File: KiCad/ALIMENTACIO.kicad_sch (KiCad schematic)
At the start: 9 parts, among them J1 Conn_01x02_Pin, U1 LM2596S-5, U2 LM1117DT-3.3

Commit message: Canvis a la part d'alimentació
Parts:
- L1: value 33uH -> 100uH
- renumbered C2 to C3, U2 to U1
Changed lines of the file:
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@@
 		)
 		(instances
+			(project "ALIMENTACIO"
+				(path "/45cfcaa5-e694-40cb-923c-70f0cad76365"
+					(reference "C3")
+					(unit 1)
+				)
+			)
 			(project ""
 				(path "/b6401b4f-5426-49b8-bb2e-8ecdb19989ef/67d546eb-b5d9-4a2c-a3ee-41df96785a31"
@@
 		)
 		(instances
+			(project "ALIMENTACIO"
+				(path "/45cfcaa5-e694-40cb-923c-70f0cad76365"
+					(reference "U1")
+					(unit 1)
+				)
+			)
 			(project ""
 				(path "/b6401b4f-5426-49b8-bb2e-8ecdb19989ef/67d546eb-b5d9-4a2c-a3ee-41df96785a31"
@@
 		)
 		(instances
+			(project "ALIMENTACIO"
+				(path "/45cfcaa5-e694-40cb-923c-70f0cad76365"
+					(reference "D1")
+					(unit 1)
+				)
+			)
 			(project ""
 				(path "/b6401b4f-5426-49b8-bb2e-8ecdb19989ef/67d546eb-b5d9-4a2c-a3ee-41df96785a31"
@@
 		)
 		(instances
+			(project "ALIMENTACIO"
+				(path "/45cfcaa5-e694-40cb-923c-70f0cad76365"
+					(reference "C1")
+					(unit 1)
+				)
+			)
 			(project ""
 				(path "/b6401b4f-5426-49b8-bb2e-8ecdb19989ef/67d546eb-b5d9-4a2c-a3ee-41df96785a31"
@@
 		)
 		(instances
+			(project "ALIMENTACIO"
+				(path "/45cfcaa5-e694-40cb-923c-70f0cad76365"
+					(reference "J1")
+					(unit 1)
+				)
+			)
 			(project ""
 				(path "/b6401b4f-5426-49b8-bb2e-8ecdb19989ef/67d546eb-b5d9-4a2c-a3ee-41df96785a31"
@@
 		)
 		(instances
+			(project "ALIMENTACIO"
+				(path "/45cfcaa5-e694-40cb-923c-70f0cad76365"
+					(reference "C4")
+					(unit 1)
+				)
+			)
 			(project "SEIENTS_EDD"
 				(path "/b6401b4f-5426-49b8-bb2e-8ecdb19989ef/67d546eb-b5d9-4a2c-a3ee-41df96785a31"
@@
 		(dnp no)
 		(property "Reference" "L1"
-			(at 135.89 100.33 90)
-			(effects
-				(font
-					(size 1.27 1.27)
-				)
-			)
-		)
-		(property "Value" "33uH"
-			(at 129.54 102.87 90)
+			(at 135.89 108.458 90)
+			(effects
+				(font
+					(size 1.27 1.27)
+				)
+			)
+		)
+		(property "Value" "100uH"
+			(at 135.636 111.252 90)
 			(effects
 				(font
@@
 		)
 		(instances
+			(project "ALIMENTACIO"
+				(path "/45cfcaa5-e694-40cb-923c-70f0cad76365"
+					(reference "L1")
+					(unit 1)
+				)
+			)
 			(project ""
 				(path "/b6401b4f-5426-49b8-bb2e-8ecdb19989ef/67d546eb-b5d9-4a2c-a3ee-41df96785a31"
@@
 		(dnp no)
 		(fields_autoplaced yes)
-		(property "Reference" "U2"
+		(property "Reference" "U1"
 			(at 201.93 99.06 0)
 			(effects
@@
 		)
 		(instances
+			(project "ALIMENTACIO"
+				(path "/45cfcaa5-e694-40cb-923c-70f0cad76365"
+					(reference "U1")
+					(unit 1)
+				)
+			)
 			(project ""
 				(path "/b6401b4f-5426-49b8-bb2e-8ecdb19989ef/67d546eb-b5d9-4a2c-a3ee-41df96785a31"
@@
 		(dnp no)
 		(fields_autoplaced yes)
-		(property "Reference" "C2"
+		(property "Reference" "C3"
 			(at 151.13 111.7599 0)
 			(effects
@@
 		)
 		(instances
+			(project "ALIMENTACIO"
+				(path "/45cfcaa5-e694-40cb-923c-70f0cad76365"
+					(reference "C3")
+					(unit 1)
+				)
+			)
 			(project "SEIENTS_EDD"
 				(path "/b6401b4f-5426-49b8-bb2e-8ecdb19989ef/67d546eb-b5d9-4a2c-a3ee-41df96785a31"
@@
 		)
 	)
+	(sheet_instances
+		(path "/"
+			(page "1")
+		)
+	)
+	(embedded_fonts no)
 )

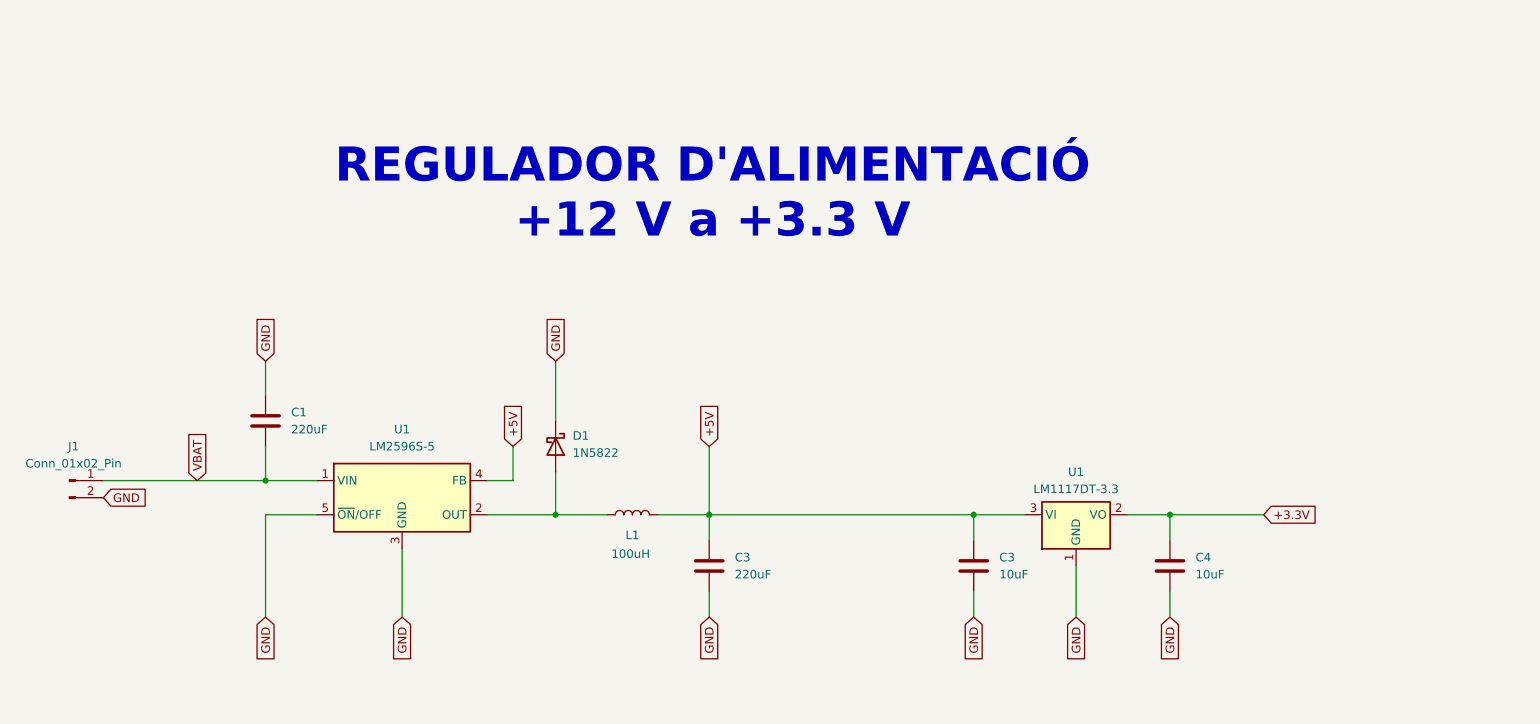
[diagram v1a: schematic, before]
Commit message: Canvis a l'alimentació: afegits TVS i Fusible
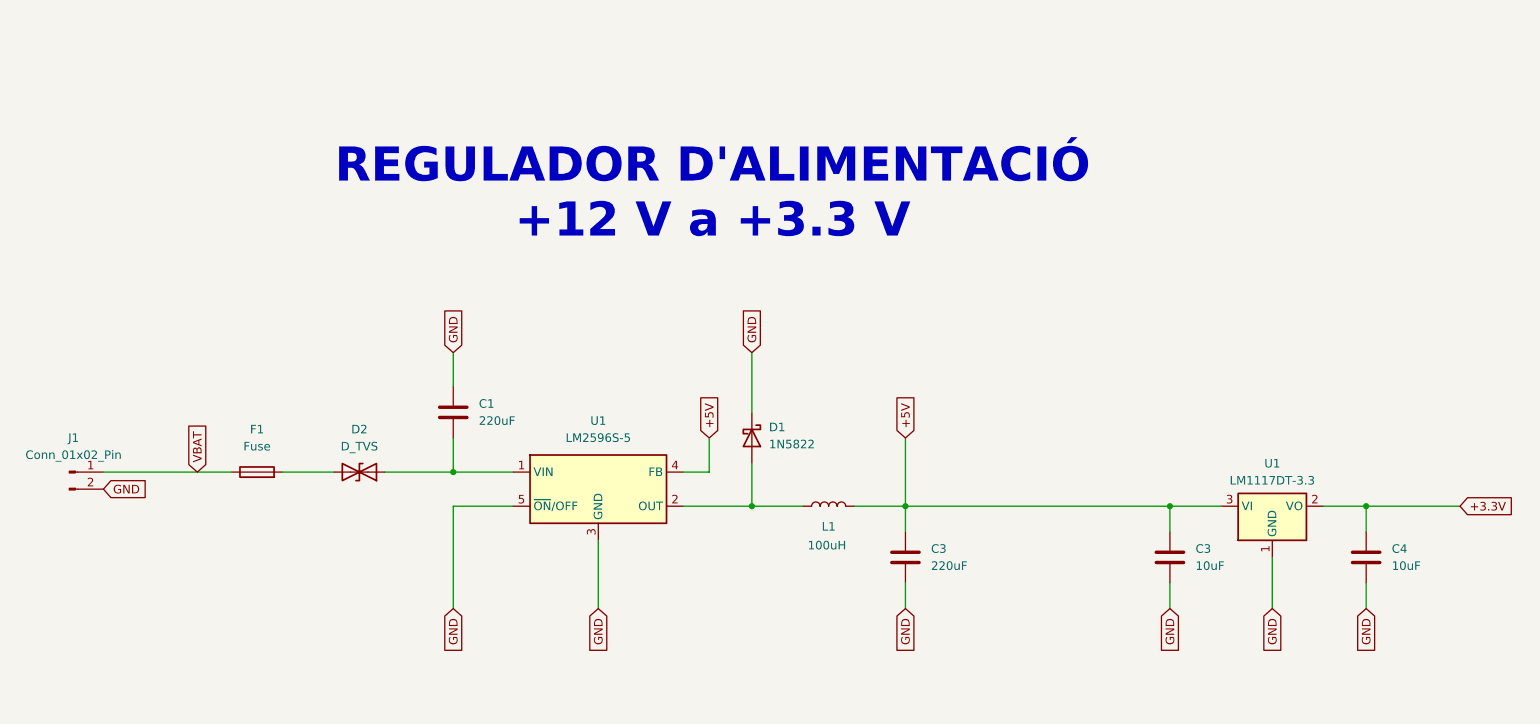
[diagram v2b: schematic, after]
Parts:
- added D2: D_TVS, symbol Device:D_TVS
- added F1: Fuse, symbol Device:Fuse
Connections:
- net VBAT: now also F1.1; no longer C1.2, U1.1 (VIN)
- new net: C1.2, D2.1 (A1), U1.1 (VIN)
- new net: D2.2 (A2), F1.2
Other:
- moved on the sheet: C1, C3, C4, D1, J1, L1, U1

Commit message: Canvis a l'alimentació: afegides capacitats de desacoblament
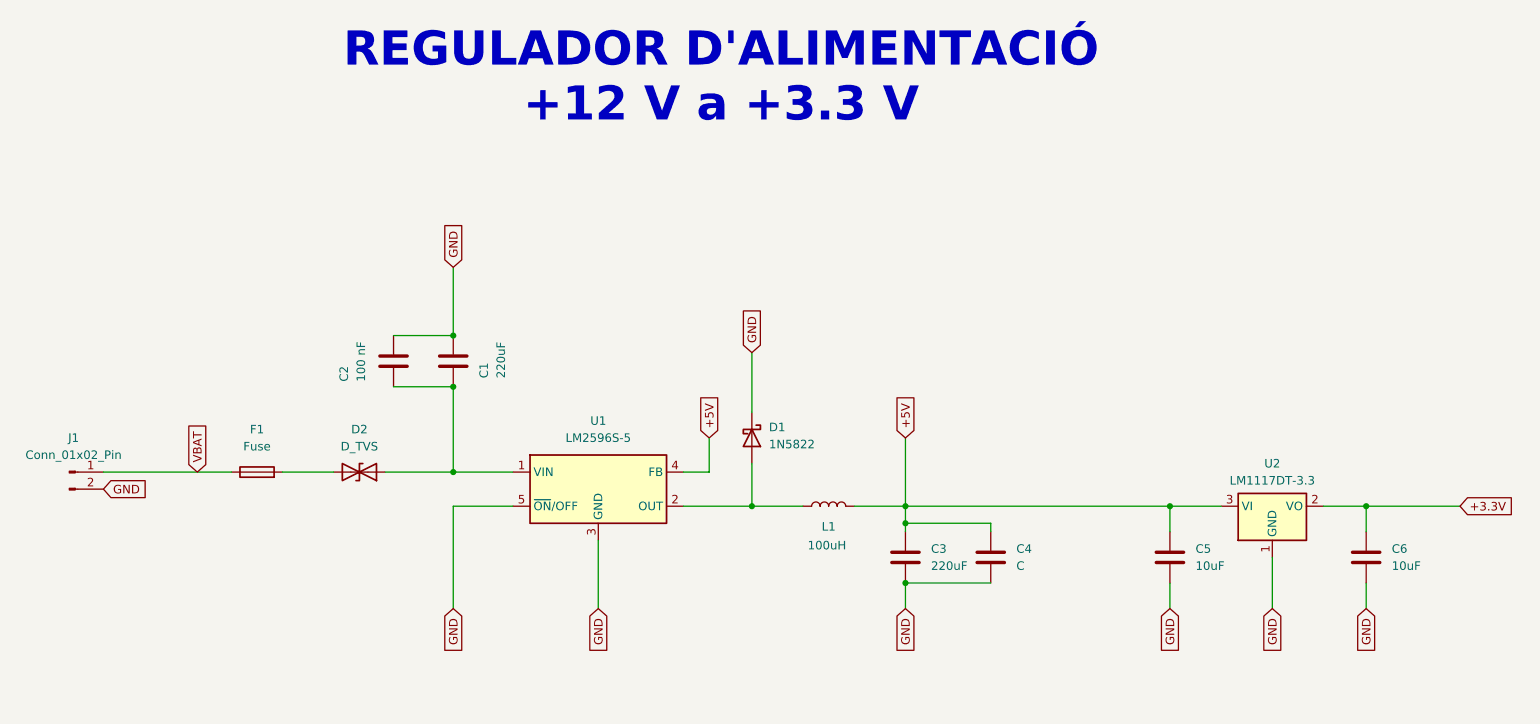
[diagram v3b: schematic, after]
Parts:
- added C2: 100 nF, symbol Device:C
- added C4: C, symbol Device:C
- renumbered C3 to C5, C4 to C6, U1 to U2
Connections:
- net +5V: now also C4.1
- net GND: now also C2.1, C4.2
- net at C1.2, D2.1 (A1), U1.1 (VIN): now also C2.2
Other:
- moved on the sheet: C1
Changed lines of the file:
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@@
 	(text "REGULADOR D'ALIMENTACIÓ\n+12 V a +3.3 V"
 		(exclude_from_sim no)
-		(at 147.828 57.658 0)
+		(at 149.098 40.386 0)
 		(effects
 			(font
@@
 	)
 	(junction
+		(at 109.22 78.74)
+		(diameter 0)
+		(color 0 0 0 0)
+	)
+	(junction
 		(at 109.22 99.06)
 		(diameter 0)
@@
 	)
 	(junction
+		(at 176.53 106.68)
+		(diameter 0)
+		(color 0 0 0 0)
+	)
+	(junction
+		(at 176.53 115.57)
+		(diameter 0)
+		(color 0 0 0 0)
+	)
+	(junction
+		(at 109.22 86.36)
+		(diameter 0)
+		(color 0 0 0 0)
+	)
+	(junction
 		(at 215.9 104.14)
 		(diameter 0)
@@
 	(wire
 		(pts
+			(xy 189.23 106.68) (xy 176.53 106.68)
+		)
+		(stroke
+			(width 0)
+			(type default)
+		)
+	)
+	(wire
+		(pts
 			(xy 57.15 99.06) (xy 76.2 99.06)
 		)
@@
 	(wire
 		(pts
+			(xy 189.23 107.95) (xy 189.23 106.68)
+		)
+		(stroke
+			(width 0)
+			(type default)
+		)
+	)
+	(wire
+		(pts
 			(xy 143.51 99.06) (xy 147.32 99.06)
 		)
@@
 	(wire
 		(pts
+			(xy 176.53 115.57) (xy 189.23 115.57)
+		)
+		(stroke
+			(width 0)
+			(type default)
+		)
+	)
+	(wire
+		(pts
 			(xy 109.22 119.38) (xy 109.22 104.14)
 		)
@@
 	(wire
 		(pts
-			(xy 176.53 107.95) (xy 176.53 104.14)
+			(xy 176.53 107.95) (xy 176.53 106.68)
 		)
 		(stroke
@@
 	(wire
 		(pts
+			(xy 100.33 86.36) (xy 109.22 86.36)
+		)
+		(stroke
+			(width 0)
+			(type default)
+		)
+	)
+	(wire
+		(pts
 			(xy 83.82 99.06) (xy 91.44 99.06)
 		)
@@
 	(wire
 		(pts
-			(xy 109.22 93.98) (xy 109.22 99.06)
+			(xy 109.22 86.36) (xy 109.22 99.06)
 		)
 		(stroke
@@
 	(wire
 		(pts
+			(xy 176.53 106.68) (xy 176.53 104.14)
+		)
+		(stroke
+			(width 0)
+			(type default)
+		)
+	)
+	(wire
+		(pts
 			(xy 153.67 81.28) (xy 153.67 90.17)
 		)
@@
 	(wire
 		(pts
-			(xy 109.22 81.28) (xy 109.22 86.36)
+			(xy 109.22 68.58) (xy 109.22 78.74)
+		)
+		(stroke
+			(width 0)
+			(type default)
+		)
+	)
+	(wire
+		(pts
+			(xy 100.33 78.74) (xy 109.22 78.74)
 		)
 		(stroke
@@
 	(global_label "GND"
 		(shape input)
-		(at 109.22 81.28 90)
+		(at 109.22 68.58 90)
 		(fields_autoplaced yes)
 		(effects
@@
 		)
 		(property "Intersheetrefs" "${INTERSHEET_REFS}"
-			(at 109.22 74.4243 90)
+			(at 109.22 61.7243 90)
 			(effects
 				(font
@@
 		(dnp no)
 		(fields_autoplaced yes)
-		(property "Reference" "C3"
+		(property "Reference" "C5"
 			(at 219.71 110.4899 0)
 			(effects
@@
 			(project "ALIMENTACIO"
 				(path "/45cfcaa5-e694-40cb-923c-70f0cad76365"
-					(reference "C3")
+					(reference "C5")
 					(unit 1)
 				)
@@
 	(symbol
 		(lib_id "Device:C")
-		(at 109.22 90.17 0)
+		(at 109.22 82.55 0)
 		(unit 1)
 		(exclude_from_sim no)
@@
 		(on_board yes)
 		(dnp no)
-		(fields_autoplaced yes)
 		(property "Reference" "C1"
-			(at 113.03 88.8999 0)
+			(at 113.792 85.09 90)
 			(effects
 				(font
@@
 		)
 		(property "Value" "220uF"
-			(at 113.03 91.4399 0)
+			(at 116.332 85.09 90)
 			(effects
 				(font
@@
 		)
 		(property "Footprint" ""
-			(at 110.1852 93.98 0)
+			(at 110.1852 86.36 0)
 			(effects
 				(font
@@
 		)
 		(property "Datasheet" "~"
-			(at 109.22 90.17 0)
+			(at 109.22 82.55 0)
 			(effects
 				(font
@@
 		)
 		(property "Description" "Unpolarized capacitor"
-			(at 109.22 90.17 0)
+			(at 109.22 82.55 0)
 			(effects
 				(font
@@
 		(dnp no)
 		(fields_autoplaced yes)
-		(property "Reference" "C4"
+		(property "Reference" "C6"
 			(at 248.92 110.4899 0)
 			(effects
@@
 			(project "ALIMENTACIO"
 				(path "/45cfcaa5-e694-40cb-923c-70f0cad76365"
-					(reference "C4")
+					(reference "C6")
 					(unit 1)
 				)
@@
 			(project "SEIENTS_EDD"
 				(path "/b6401b4f-5426-49b8-bb2e-8ecdb19989ef/67d546eb-b5d9-4a2c-a3ee-41df96785a31"
+					(reference "C4")
+					(unit 1)
+				)
+			)
+		)
+	)
+	(symbol
+		(lib_id "Device:C")
+		(at 100.33 82.55 0)
+		(unit 1)
+		(exclude_from_sim no)
+		(in_bom yes)
+		(on_board yes)
+		(dnp no)
+		(property "Reference" "C2"
+			(at 92.964 85.598 90)
+			(effects
+				(font
+					(size 1.27 1.27)
+				)
+				(justify left)
+			)
+		)
+		(property "Value" "100 nF"
+			(at 95.504 85.598 90)
+			(effects
+				(font
+					(size 1.27 1.27)
+				)
+				(justify left)
+			)
+		)
+		(property "Footprint" ""
+			(at 101.2952 86.36 0)
+			(effects
+				(font
+					(size 1.27 1.27)
+				)
+				(hide yes)
+			)
+		)
+		(property "Datasheet" "~"
+			(at 100.33 82.55 0)
+			(effects
+				(font
+					(size 1.27 1.27)
+				)
+				(hide yes)
+			)
+		)
+		(property "Description" "Unpolarized capacitor"
+			(at 100.33 82.55 0)
+			(effects
+				(font
+					(size 1.27 1.27)
+				)
+				(hide yes)
+			)
+		)
+		(pin "2"
+		)
+		(pin "1"
+		)
+		(instances
+			(project ""
+				(path "/45cfcaa5-e694-40cb-923c-70f0cad76365"
+					(reference "C2")
+					(unit 1)
+				)
+			)
+		)
+	)
+	(symbol
+		(lib_id "Device:C")
+		(at 189.23 111.76 0)
+		(unit 1)
+		(exclude_from_sim no)
+		(in_bom yes)
+		(on_board yes)
+		(dnp no)
+		(fields_autoplaced yes)
+		(property "Reference" "C4"
+			(at 193.04 110.4899 0)
+			(effects
+				(font
+					(size 1.27 1.27)
+				)
+				(justify left)
+			)
+		)
+		(property "Value" "C"
+			(at 193.04 113.0299 0)
+			(effects
+				(font
+					(size 1.27 1.27)
+				)
+				(justify left)
+			)
+		)
+		(property "Footprint" ""
+			(at 190.1952 115.57 0)
+			(effects
+				(font
+					(size 1.27 1.27)
+				)
+				(hide yes)
+			)
+		)
+		(property "Datasheet" "~"
+			(at 189.23 111.76 0)
+			(effects
+				(font
+					(size 1.27 1.27)
+				)
+				(hide yes)
+			)
+		)
+		(property "Description" "Unpolarized capacitor"
+			(at 189.23 111.76 0)
+			(effects
+				(font
+					(size 1.27 1.27)
+				)
+				(hide yes)
+			)
+		)
+		(pin "2"
+		)
+		(pin "1"
+		)
+		(instances
+			(project ""
+				(path "/45cfcaa5-e694-40cb-923c-70f0cad76365"
 					(reference "C4")
 					(unit 1)
@@
 		(dnp no)
 		(fields_autoplaced yes)
-		(property "Reference" "U1"
+		(property "Reference" "U2"
 			(at 231.14 97.79 0)
 			(effects
@@
 			(project "ALIMENTACIO"
 				(path "/45cfcaa5-e694-40cb-923c-70f0cad76365"
-					(reference "U1")
-					(unit 1)
-				)
+					(reference "U2")
+					(unit 1)
+				)

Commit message: Canvis a l'alimentació: Problemes ERC solventats
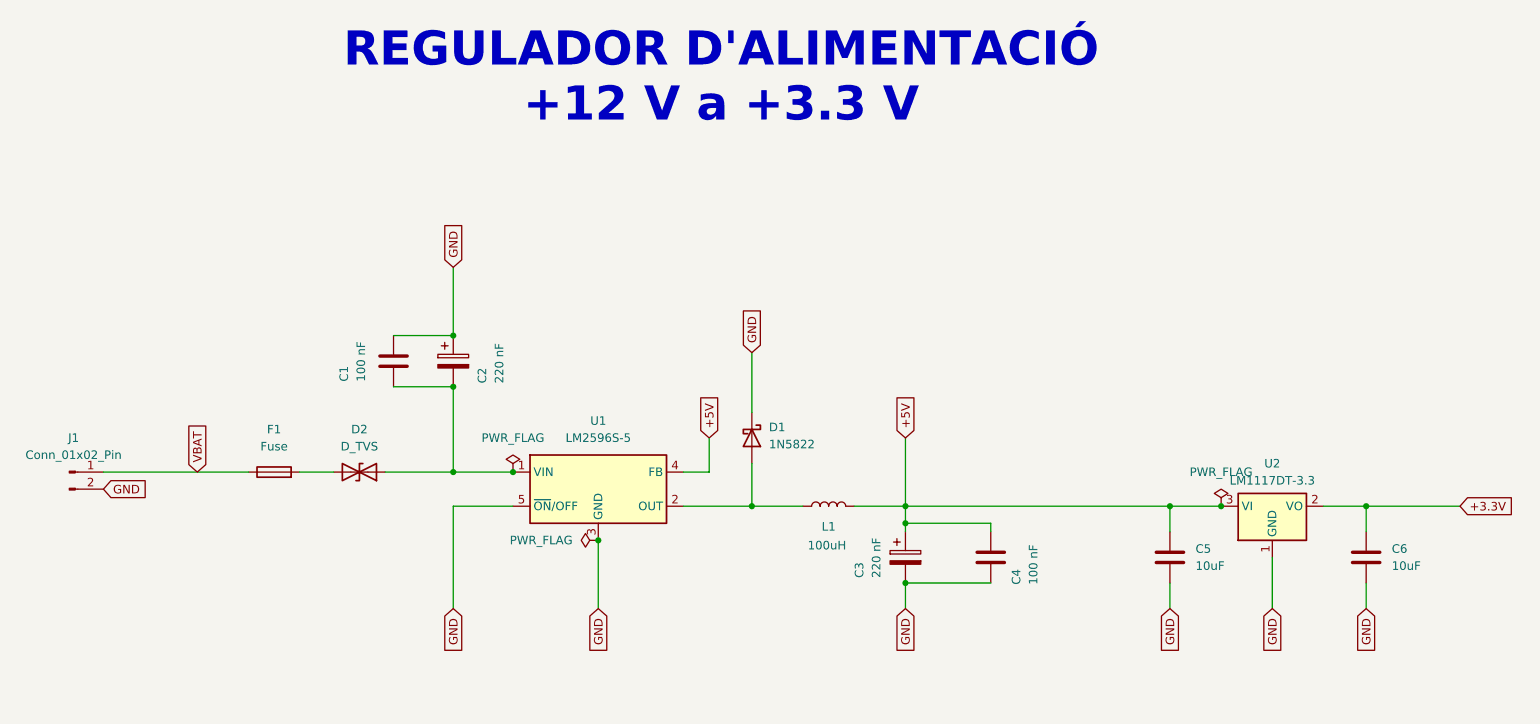
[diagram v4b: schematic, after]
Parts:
- removed C1, C3: 220uF, symbol Device:C
- added C2, C3: 220 nF, symbol Device:C_Polarized
- C4: value C -> 100 nF
- renumbered C2 to C1
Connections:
- net +5V: now also C3.1
- net GND: now also C2.1, C3.2
- net at C1.2, D2.1 (A1), U1.1 (VIN): now also C2.2
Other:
- moved on the sheet: F1

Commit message: Canvis a l'alimentació: part acabada
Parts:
- C2, C3: value 220 nF -> 220 uF
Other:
- moved on the sheet: D1
